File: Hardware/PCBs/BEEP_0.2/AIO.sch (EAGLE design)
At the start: 88 parts, among them IC1 74HC238SSOP, IC2 74HC238SSOP, IC3 ULN2803ASOP18, IC4 ULN2803ASOP18, IC5 TS34119SMD, Q1 DMN2075U, Q2 DMN2075U, Q3 DMN2075U, Q4 DMN2075U, Q5 DMN2075U, Q6 32Mhz, U1 ATXMEGA64D3-AU, U2 TB6612FNG, X1 Sens1, X10 exp header, X11 MICROMATCH-10, X12 MICROMATCH-4, X13 MICROMATCH-4, X2 Sens2, X3 MICROMATCH-8, X4 MICROMATCH-8, X5 PDI interface (ISP), X6 Sens5, X7 Sens6, X8 MICROMATCH-8, X9 MICROMATCH-8

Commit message: minor enhancements
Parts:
- removed U$10, U$11, U$12, U$9: CNY70, BEEP:CNY70
- removed U$7: RASPBERRY-PI, BEEP:RASPBERRY-PI
- removed U$8: DMC3028LSD, BEEP:DMC3028LSD
- removed U1: ATXMEGA64D3-AU, atmel-xmega:ATXMEGA64D3-AU
- removed U2: TB6612FNG, SparkFun-PowerIC:TB6621FNG
- added D1, D2, D3, D4: CNY70, BEEP:CNY70
- added IC7: TB6612FNG, SparkFun-PowerIC:TB6621FNG
- added IC8: TS34119SMD, BEEP:TS34119SMD
- added IC9: RASPBERRY-PI, BEEP:RASPBERRY-PI
- added Q7: DMC3028LSD, BEEP:DMC3028LSD
- C10, C15: value 1uF -> 100nF
- C11: value 10uF -> 100nF; device rcl:CPOL-EUSMCD -> rcl:C-EUC0603
- C12: value 10uF -> 1uF; device rcl:CPOL-EUSMCD -> rcl:C-EUC0603
- C13, C14: value 100nF -> 10uF; device rcl:C-EUC0603 -> rcl:CPOL-EUSMCD
- C16: value 22pF -> 100nF
- C17: value 22pF -> 1uF
- C7, C8: value 100nF -> 22pF
- IC5: value TS34119SMD -> ATXMEGA64D3-AU; device BEEP:TS34119SMD -> atmel-xmega:ATXMEGA64D3-AU
- Q4: value DMN2075U -> 32Mhz; device BEEP:DMN2075U -> crystal:CRYSTALHC49S
- Q6: value 32Mhz -> DMN2075U; device crystal:CRYSTALHC49S -> BEEP:DMN2075U
- R11: value 10k -> 100R
- R12: value 220R -> 10k
- R13: value 390R -> 220R
- R14: value 100R -> 390R
- R15: value (none) -> 100R
- R16: device rcl:R-EU_R0603 -> resistor:R-EU_M0805
- R17: value 3k -> (none); device rcl:R-EU_R0603 -> resistor:R-EU_M0805
- R18: value 75k -> 3k
- R19: value 1K -> 75k
- R20: value 10k -> 1K
- R21: value 100k -> (none); device rcl:R-EU_R0603 -> resistor:R-EU_M0805
- R22, R25, R26, R28, R29, R4, R5, R6: device rcl:R-EU_R0805 -> resistor:R-EU_M0805
- R23, R30: value (none) -> 10k; device rcl:R-EU_R0805 -> rcl:R-EU_R0603
- R24: value 10k -> 100k
- R27: value (none) -> 0R; device rcl:R-EU_R0805 -> rcl:R-EU_R0603
- R31: value 0R -> (none); device rcl:R-EU_R0603 -> resistor:R-EU_M0805
- R32: value 100R -> (none); device rcl:R-EU_R0603 -> resistor:R-EU_M0805
- R8, R9: device rcl:R-EU_R0603 -> rcl:R-EU_M0805
- renumbered U$5 to IC6
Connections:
- net +3V3: now also C10.2, C13.-, C15.2, C9.2, D1.T_C, D2.T_C, D3.T_C, D4.T_C, IC5.AVCC, IC5.VCC, IC7.VCC, IC9.+3V3, R12.1; no longer C11.-, C13.2, C7.2, C8.2, R11.1, U$10.T_C, U$11.T_C, U$12.T_C, U$7.+3V3, U$9.T_C, U1.AVCC, U1.VCC, U2.VCC
- net +5V: now also IC8.VCC, IC9.+5V, R31.2, R32.2; no longer IC5.VCC, R29.2, R30.2, U$7.+5V
- net +7V: now also C14.-, C16.2, IC7.VM1, IC7.VM2, IC7.VM3, Q7.D2, R16.1, R27.2, R30.1; no longer C12.-, C14.2, R15.1, R24.1, R31.2, U$8.D2, U2.VM1, U2.VM2, U2.VM3
- net ADISTANCE_0: now also IC5.PB0; no longer U1.PB0
- net ADISTANCE_1: now also IC5.PB1; no longer U1.PB1
- net ADISTANCE_2: now also IC5.PB2; no longer U1.PB2
- net ADISTANCE_3: now also IC5.PB3; no longer U1.PB3
- net ADISTANCE_4: now also IC5.PB4; no longer U1.PB4
- net ADISTANCE_5: now also IC5.PB5; no longer U1.PB5
- net ADISTANCE_6: now also IC5.PB6; no longer U1.PB6
- net ADISTANCE_7: now also IC5.PB7; no longer U1.PB7
- net AUDIO_DISABLE: now also IC5.PF6, IC8.CD; no longer IC5.CD, U1.PF6
- net AUDIO_IN: now also C11.2; no longer C9.2
- net BATT_GND: now also Q6.D; no longer Q4.D
- net BATT_U: now also Q7.S2, R15.1, R23.1, R27.1; no longer R14.1, R20.1, R31.1, U$8.S2
- net BATT_VOLTAGE: now also IC5.PA2, R16.2, R17.1; no longer R15.2, R16.1, U1.PA2
- net BATT_WARN_0: now also IC5.PA3, R13.1; no longer R12.1, U1.PA3
- net BATT_WARN_1: now also IC5.PA4, R14.1; no longer R13.1, U1.PA4
- net COLOR_DIODE_1: now also IC5.PD5; no longer U1.PD5
- net COLOR_DIODE_2: now also IC5.PD6; no longer U1.PD6
- net COLOR_FREQ_OUT: now also IC5.PD0; no longer U1.PD0
- net COLOR_SENSOR_1: now also IC5.PD7; no longer U1.PD7
- net COLOR_SENSOR_2: now also IC5.PD1; no longer U1.PD1
- net COLOR_SENSOR_3: now also IC5.PD4; no longer U1.PD4
- net COLOR_SENSOR_PWM_LED: now also IC5.PE3, R11.1; no longer R32.1, U1.PE3
- net ENCODER_L1: now also D2.T_E; no longer U$9.T_E
- net ENCODER_L2: now also D4.T_E, R29.2; no longer R27.2, U$11.T_E
- net ENCODER_R1: now also D1.T_E, R21.2; no longer R23.2, U$10.T_E
- net ENCODER_R2: now also D3.T_E; no longer U$12.T_E
- net GND: now also C10.1, C12.2, C13.+, C14.+, C15.1, C17.2, C9.1, D1.LED_C, D2.LED_C, D3.LED_C, D4.LED_C, IC5.PA1, IC7.GND, IC7.PGND1@3, IC7.PGND1@4, IC7.PGND2@10, IC7.PGND2@9, IC8.GND, IC9.GND, Q6.S, Q7.S1, R17.2, R20.2, R21.1, R29.1; no longer C10.2, C11.+, C12.+, C13.1, C14.1, C15.2, C17.1, Q4.S, R16.2, R19.2, R23.1, R27.1, U$10.LED_C, U$11.LED_C, U$12.LED_C, U$7.GND, U$8.S1, U$9.LED_C, U1.GND, U1.PA1, U2.GND, U2.PGND1@3, U2.PGND1@4, U2.PGND2@10, U2.PGND2@9
- net IR_LED_MK0: now also IC5.PF0; no longer U1.PF0
- net IR_LED_MK1: now also IC5.PF1; no longer U1.PF1
- net IR_LED_MK2: now also IC5.PF2; no longer U1.PF2
- net LED_A0: now also IC5.PE0; no longer U1.PE0
- net LED_A1: now also IC5.PE1; no longer U1.PE1
- net LED_A2: now also IC5.PE2; no longer U1.PE2
- net MOTOR_A_IN1: now also IC5.PE5, IC7.AIN1; no longer U1.PE5, U2.AIN1
- net MOTOR_A_IN2: now also IC5.PE4, IC7.AIN2; no longer U1.PE4, U2.AIN2
- net MOTOR_A_OUT1: now also IC7.A01@1, IC7.A01@2; no longer U2.A01@1, U2.A01@2
- net MOTOR_A_OUT2: now also IC7.A02@5, IC7.A02@6; no longer U2.A02@5, U2.A02@6
- net MOTOR_A_PWM: now also IC5.PC3, IC7.PWMA; no longer U1.PC3, U2.PWMA
- net MOTOR_B_IN1: now also IC5.PE6, IC7.BIN1; no longer U1.PE6, U2.BIN1
- net MOTOR_B_IN2: now also IC5.PE7, IC7.BIN2; no longer U1.PE7, U2.BIN2
- net MOTOR_B_OUT1: now also IC7.B01@11, IC7.B01@12; no longer U2.B01@11, U2.B01@12
- net MOTOR_B_OUT2: now also IC7.B02@7, IC7.B02@8; no longer U2.B02@7, U2.B02@8
- net MOTOR_B_PWM: now also IC5.PC2, IC7.PWMB; no longer U1.PC2, U2.PWMB
- net MOTOR_STBY: now also IC5.PC6, IC7.STBY; no longer U1.PC6, U2.STBY
- net N$11: now also D4.LED_A, R32.1; no longer R29.1, U$11.LED_A
- net N$14: now also C8.2, IC5.PR1, Q4.1; no longer C17.2, Q6.1, U1.PR1
- net N$15: now also IC8.VIN, R18.1, R19.2; no longer IC5.VIN, R17.1, R18.2
- net N$16: now also C17.1, R24.2; no longer C15.1, R21.2
- net N$17: now also C11.1, R18.2; no longer C9.1, R17.2
- net N$18: now also C7.2, IC5.PR0, Q4.2; no longer C16.2, Q6.2, U1.PR0
- net N$19: now also R20.1; no longer R19.1
- net N$20: now also D1.LED_A, R25.1; no longer R26.1, U$10.LED_A
- net N$22: now also Q7.D1, Q7.G2, R23.2, R24.1; no longer R20.2, R21.1, U$8.D1, U$8.G2
- net N$23: now also D2.LED_A, R26.1; no longer R25.1, U$9.LED_A
- net N$25: now also R11.2; no longer R32.2
- net N$26: now also D3.LED_A, R31.1; no longer R30.1, U$12.LED_A
- net N$29: now also R14.2; no longer R13.2
- net N$32: now also R13.2; no longer R12.2
- net N$36: now also C12.1, IC8.FC2; no longer C10.1, IC5.FC2
- net N$4: now also IC5.PA0; no longer U1.PA0
- net N$8: now also Q6.G, R15.2; no longer Q4.G, R14.2
- net PDI_CLK: now also IC5.!RESET!/PDI; no longer U1.!RESET!/PDI
- net PDI_DATA: now also IC5.PDI; no longer U1.PDI
- net POWER_OFF: now also IC5.PC7, Q7.G1, R30.2; no longer R24.2, U$8.G1, U1.PC7
- net RGB_LED_MK0: now also IC5.PF5; no longer U1.PF5
- net RGB_LED_MK1: now also IC5.PF4; no longer U1.PF4
- net RGB_LED_MK2: now also IC5.PF3; no longer U1.PF3
- net RPI_RX: now also IC5.PD3, IC9.GPIO_15; no longer U$7.GPIO_15, U1.PD3
- net RPI_TX: now also IC5.PD2, IC9.GPIO_14; no longer U$7.GPIO_14, U1.PD2
- net SCL: now also IC5.PC1, IC9.GPIO_1, R12.2; no longer R11.2, U$7.GPIO_1, U1.PC1
- net SDA: now also IC5.PC0, IC9.GPIO_0; no longer U$7.GPIO_0, U1.PC0
- net SPEAKER_O1: now also IC8.VO2; no longer IC5.VO2
- net SPEAKER_O2: now also IC8.VO1, R19.1; no longer IC5.VO1, R18.1
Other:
- note added: "TODO: *3M Stecker *Stecker codierung? *Silkscreen sortieren?"
- note removed: "TODO: *3M Stecker *Stecker codierung? *Spannungsteiler berechnen, ADC nachlesen *Silkscreen sortieren?"
- moved on the sheet: C1, C10, C15, C16, C17, C3, C7, C8, C9, IC1, IC2, IC3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

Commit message: add lib for modified micromatch connector (with orietation hole) use micromatch connector with orientation hole
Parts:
- X10, X5: device con-amp:FTOP-6 -> con-ftop-orientation-hole:FTOP-6
- X11: value MICROMATCH-10 -> (none); device Con-amp-micromatch:MICROMATCH-10 -> con-ftop-orientation-hole:FTOP-10
- X12, X13: value MICROMATCH-4 -> (none); device Con-amp-micromatch:MICROMATCH-4 -> con-ftop-orientation-hole:FTOP-4
- X3: value MICROMATCH-8 -> Sens0; device Con-amp-micromatch:MICROMATCH-8 -> con-ftop-orientation-hole:FTOP-8
- X4: value MICROMATCH-8 -> Sens3; device Con-amp-micromatch:MICROMATCH-8 -> con-ftop-orientation-hole:FTOP-8
- X8: value MICROMATCH-8 -> Sens4; device Con-amp-micromatch:MICROMATCH-8 -> con-ftop-orientation-hole:FTOP-8
- X9: value MICROMATCH-8 -> Sens7; device Con-amp-micromatch:MICROMATCH-8 -> con-ftop-orientation-hole:FTOP-8
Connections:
- net +3V3: now also X11-10.1; no longer X11-10.S
- net +5V: now also X3-1.1, X4-1.1, X8-1.1, X9-1.1; no longer X3-8.S, X4-8.S, X8-8.S, X9-8.S
- net ADISTANCE_0: now also X3-2.1; no longer X3-7.S
- net ADISTANCE_3: now also X4-2.1; no longer X4-7.S
- net ADISTANCE_4: now also X8-2.1; no longer X8-7.S
- net ADISTANCE_7: now also X9-2.1; no longer X9-7.S
- net AUDIO_IN: now also X13-4.1; no longer X13-1.S
- net COLOR_DIODE_1: now also X11-4.1; no longer X11-4.S
- net COLOR_DIODE_2: now also X11-3.1; no longer X11-3.S
- net COLOR_FREQ_OUT: now also X11-7.1; no longer X11-7.S
- net COLOR_SENSOR_1: now also X11-2.1; no longer X11-2.S
- net COLOR_SENSOR_2: now also X11-6.1; no longer X11-6.S
- net COLOR_SENSOR_3: now also X11-5.1; no longer X11-5.S
- net GND: now also X11-8.1, X13-1.1, X3-3.1, X4-3.1, X8-3.1, X9-3.1; no longer X11-8.S, X13-4.S, X3-6.S, X4-6.S, X8-6.S, X9-6.S
- net IR_LED_K0_OUT: now also X3-4.1; no longer X3-5.S
- net IR_LED_K3_OUT: now also X4-4.1; no longer X4-5.S
- net IR_LED_K4_OUT: now also X8-4.1; no longer X8-5.S
- net IR_LED_K7_OUT: now also X9-4.1; no longer X9-5.S
- net LED_A0_OUT: now also X3-8.1, X4-8.1, X8-8.1, X9-8.1; no longer X3-1.S, X4-1.S, X8-1.S, X9-1.S
- net LED_A1_OUT: now also X3-7.1, X4-7.1, X8-7.1, X9-7.1; no longer X3-2.S, X4-2.S, X8-2.S, X9-2.S
- net LED_A2_OUT: now also X3-6.1, X4-6.1, X8-6.1, X9-6.1; no longer X3-3.S, X4-3.S, X8-3.S, X9-3.S
- net LED_K0_OUT: now also X3-5.1; no longer X3-4.S
- net LED_K3_OUT: now also X4-5.1; no longer X4-4.S
- net LED_K4_OUT: now also X8-5.1; no longer X8-4.S
- net LED_K7_OUT: now also X9-5.1; no longer X9-4.S
- net MOTOR_A_OUT1: now also X12-4.1; no longer X12-1.S
- net MOTOR_A_OUT2: now also X12-3.1; no longer X12-2.S
- net MOTOR_B_OUT1: now also X12-1.1; no longer X12-4.S
- net MOTOR_B_OUT2: now also X12-2.1; no longer X12-3.S
- net N$5: now also X11-9.1; no longer X11-9.S
- net SPEAKER_O1: now also X13-2.1; no longer X13-3.S
- net SPEAKER_O2: now also X13-3.1; no longer X13-2.S
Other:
- note added: "TODO: *Silkscreen sortieren?"
- note removed: "TODO: *3M Stecker *Stecker codierung? *Silkscreen sortieren?"

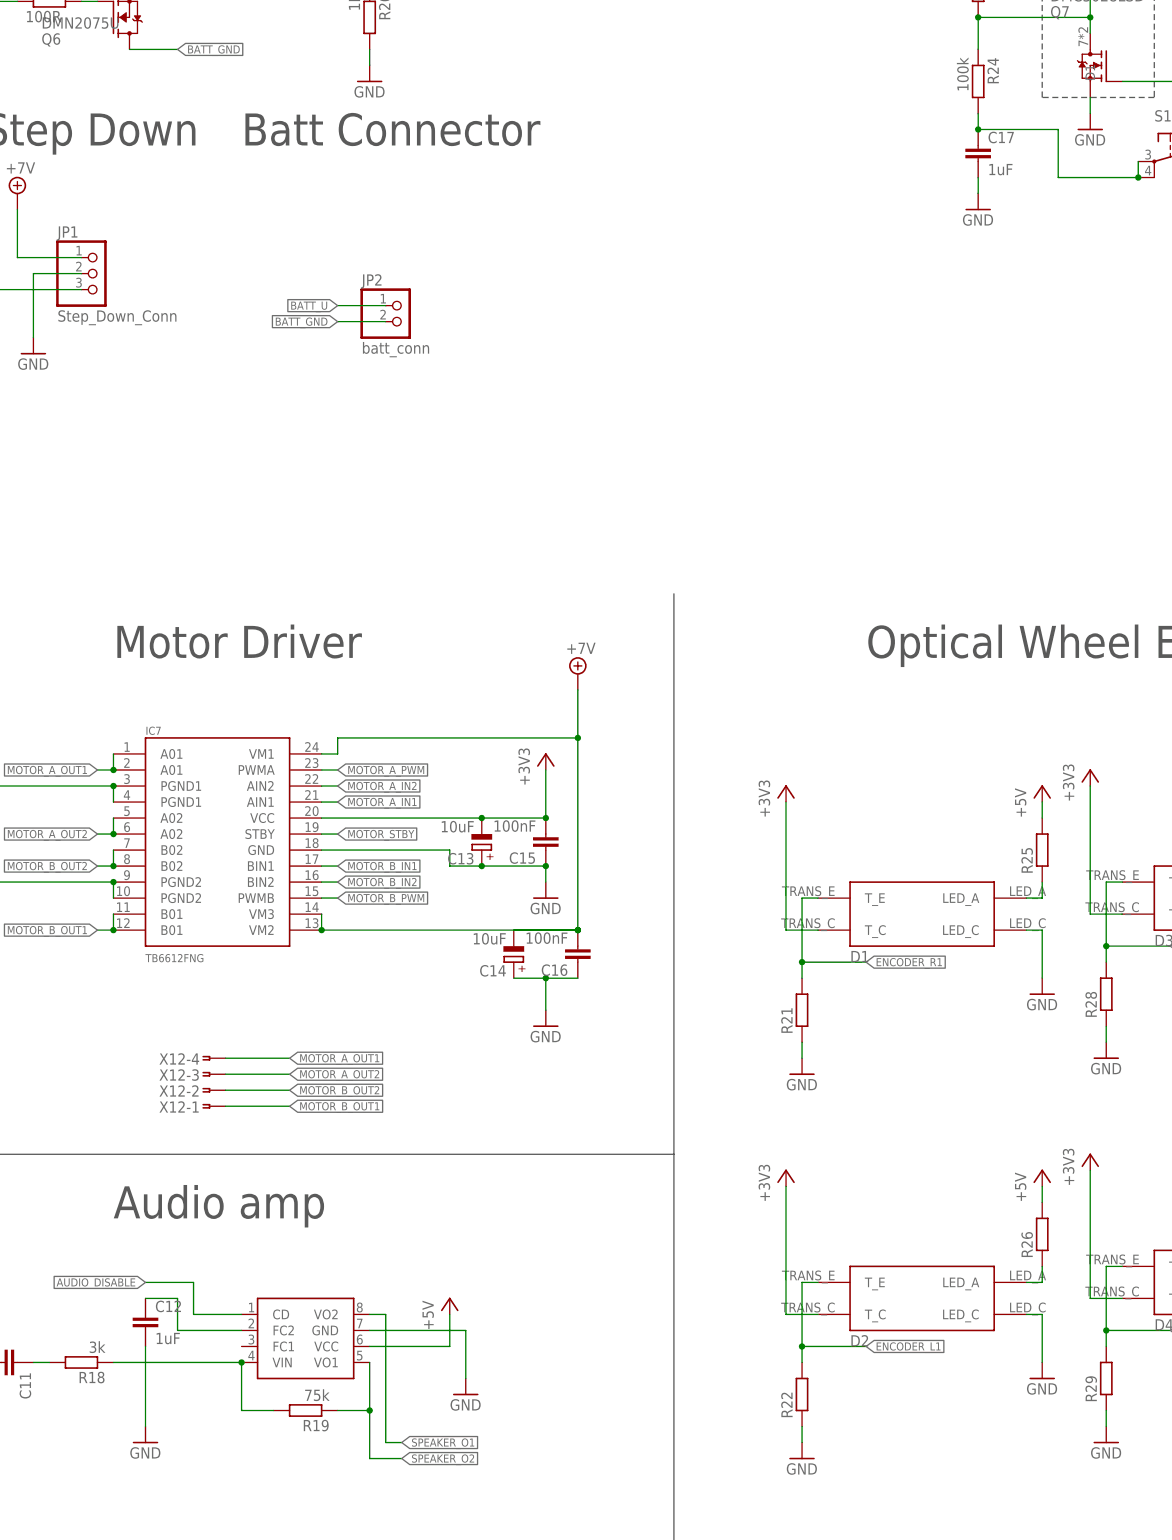
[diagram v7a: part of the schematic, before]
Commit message: change most 0603 components to 0805 change smd Typ D Footprint to THT Footprint
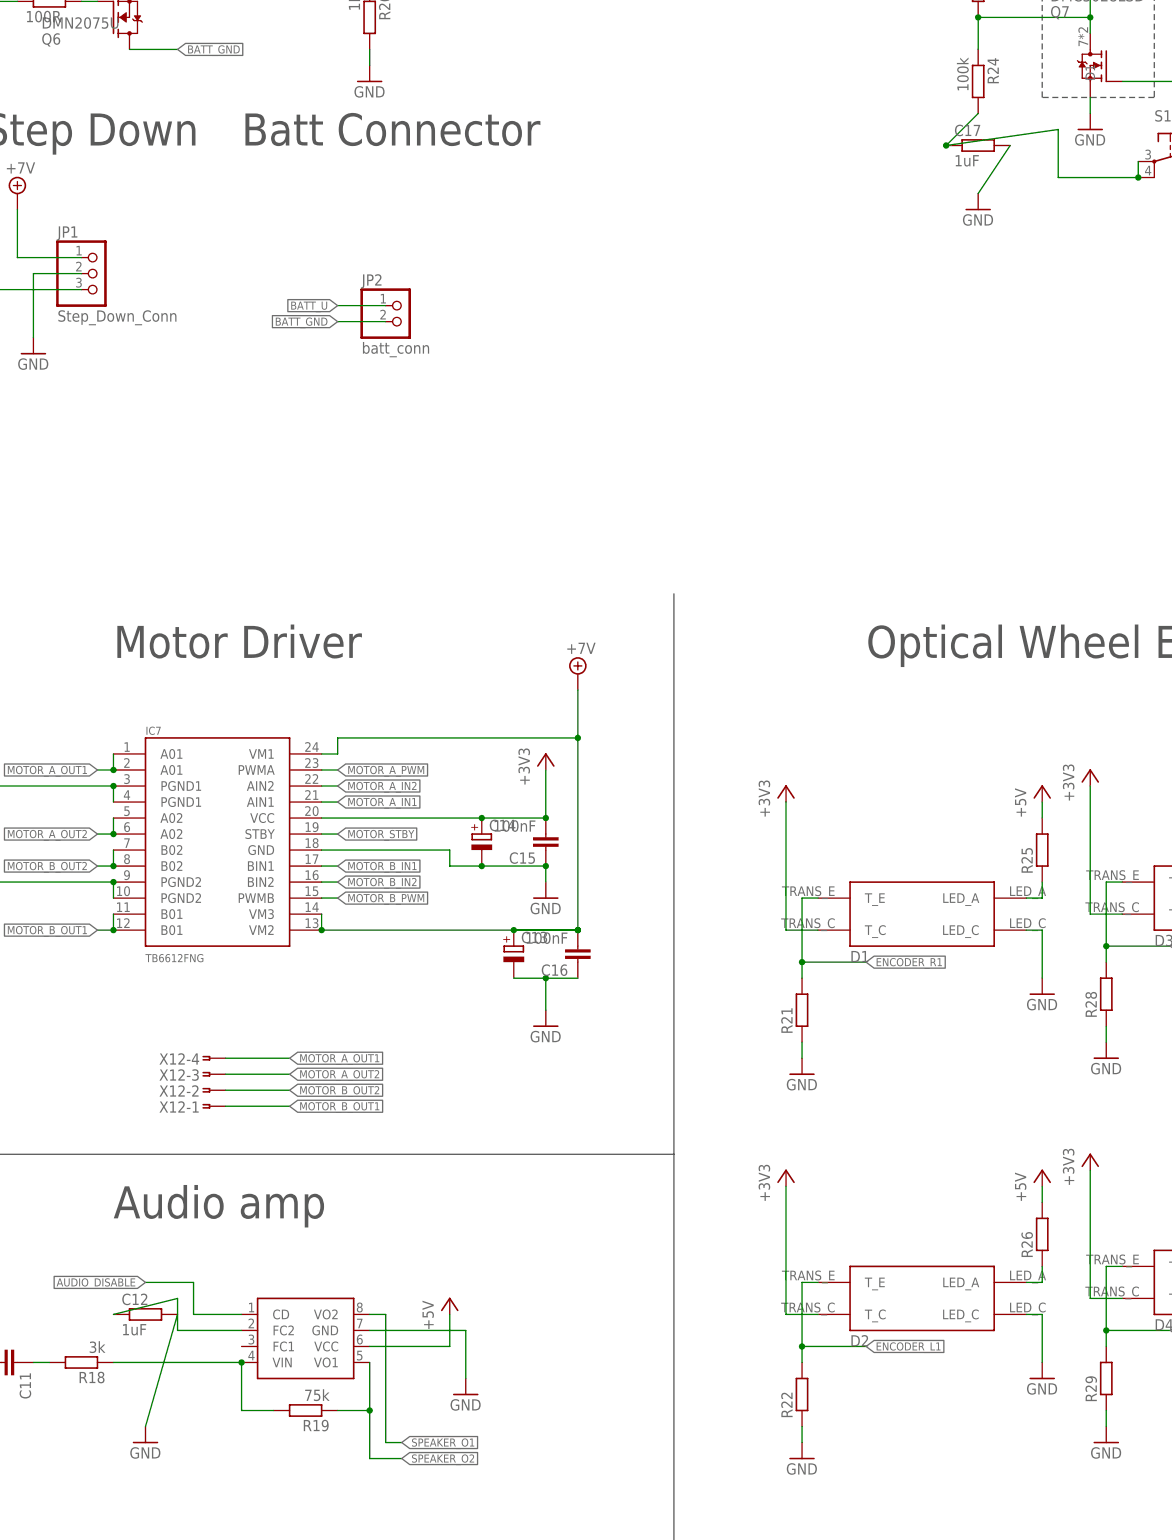
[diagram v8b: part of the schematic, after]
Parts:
- C12, C17: device rcl:C-EUC0603 -> resistor:R-EU_M0805
- C13, C14: value 10uF -> (none); device rcl:CPOL-EUSMCD -> rcl:CPOL-EUE2-5
- Q4: device crystal:CRYSTALHC49S -> crystal:CRYSTALHC18U-V
- R10, R12, R13, R14, R18, R19, R20, R23, R24, R27, R30, R7: device rcl:R-EU_R0603 -> resistor:R-EU_M0805
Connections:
- net +3V3: now also C14.+; no longer C13.-
- net +7V: now also C13.+; no longer C14.-
- net GND: now also C13.-, C14.-; no longer C13.+, C14.+
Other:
- moved on the sheet: C12, C13, C14, C17
